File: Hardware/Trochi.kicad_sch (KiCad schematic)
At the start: 61 parts, among them IC1 ICM-42688-P, J1 JST-SH, J2 JST-SH, J3 JST PH, J4 JST-SH, J5 JST-SH, J6 JST_SH, Q1 AO3401A, Q2 AO3400A, Q3 AO3400A, Q4 AO3400A, Q5 AO3400A, Q6 AO3400A, SW1 SW_SPDT, U1 ME6211C33M5, U3 YX-SMD5020

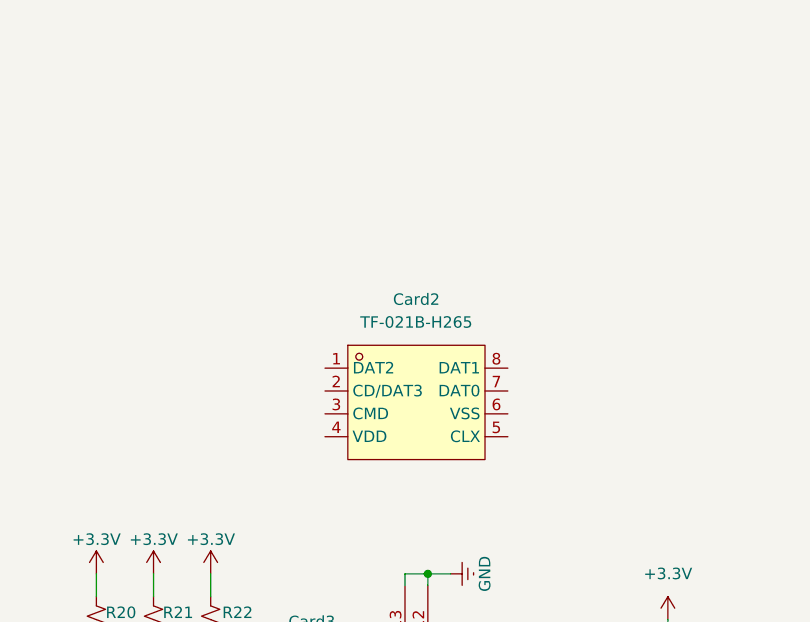
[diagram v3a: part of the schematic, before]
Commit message: feat: add updated TF-021B-H265 symbol to schematic
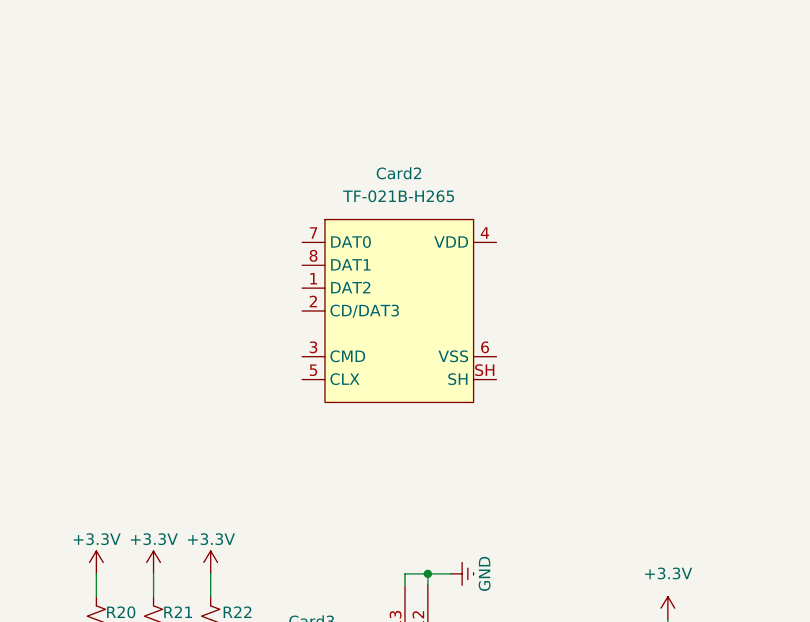
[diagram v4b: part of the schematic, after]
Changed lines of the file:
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@@
-	)
-	(symbol
-		(lib_id "trochi_sym:TF-021B-H265")
-		(at 106.68 255.27 0)
-		(unit 1)
-		(body_style 1)
-		(exclude_from_sim no)
-		(in_bom yes)
-		(on_board yes)
-		(in_pos_files yes)
-		(dnp no)
-		(fields_autoplaced yes)
-		(property "Reference" "Card2"
-			(at 102.87 243.84 0)
-			(show_name no)
-			(do_not_autoplace no)
-			(effects
-				(font
-					(size 1.27 1.27)
-				)
-			)
-		)
-		(property "Value" "TF-021B-H265"
-			(at 102.87 246.38 0)
-			(show_name no)
-			(do_not_autoplace no)
-			(effects
-				(font
-					(size 1.27 1.27)
-				)
-			)
-		)
-		(property "Footprint" "trochi_footprint:TF-SMD_TF-021B-H265"
-			(at 106.68 269.24 0)
-			(hide yes)
-			(show_name no)
-			(do_not_autoplace no)
-			(effects
-				(font
-					(size 1.27 1.27)
-				)
-			)
-		)
-		(property "Datasheet" "https://lcsc.com/product-detail/New-Arrivals_SOFNG-TF-021B-H265_C498185.html"
-			(at 106.68 271.78 0)
-			(hide yes)
-			(show_name no)
-			(do_not_autoplace no)
-			(effects
-				(font
-					(size 1.27 1.27)
-				)
-			)
-		)
-		(property "Description" ""
-			(at 106.68 255.27 0)
-			(hide yes)
-			(show_name no)
-			(do_not_autoplace no)
-			(effects
-				(font
-					(size 1.27 1.27)
-				)
-			)
-		)
-		(property "Manufacturer" "SOFNG(硕方)"
-			(at 106.68 274.32 0)
-			(hide yes)
-			(show_name no)
-			(do_not_autoplace no)
-			(effects
-				(font
-					(size 1.27 1.27)
-				)
-			)
-		)
-		(property "MPN" "TF-021B-H265"
-			(at 106.68 276.86 0)
-			(hide yes)
-			(show_name no)
-			(do_not_autoplace no)
-			(effects
-				(font
-					(size 1.27 1.27)
-				)
-			)
-		)
-		(property "LCSC Part" "C498185"
-			(at 106.68 279.4 0)
-			(hide yes)
-			(show_name no)
-			(do_not_autoplace no)
-			(effects
-				(font
-					(size 1.27 1.27)
-				)
-			)
-		)
-		(pin "1"
-		)
-		(pin "5"
-		)
-		(pin "7"
-		)
-		(pin "3"
-		)
-		(pin "4"
-		)
-		(pin "8"
-		)
-		(pin "6"
-		)
-		(pin "2"
-		)
-		(instances
-			(project "Trochi"
-				(path "/a5119cab-c33d-484e-b542-18705d0dc8d0"
-					(reference "Card2")
-					(unit 1)
-				)
-			)
-		)
 	)
 	(symbol
@@
 					(unit 1)
 				)
+			)
+		)
+	)
+	(symbol
+		(lib_id "trochi_sym:TF-021B-H265")
+		(at 104.14 243.84 0)
+		(unit 1)
+		(body_style 1)
+		(exclude_from_sim no)
+		(in_bom yes)
+		(on_board yes)
+		(in_pos_files yes)
+		(dnp no)
+		(fields_autoplaced yes)
+		(property "Reference" "Card2"
+			(at 100.965 229.87 0)
+			(show_name no)
+			(do_not_autoplace no)
+			(effects
+				(font
+					(size 1.27 1.27)
+				)
+			)
+		)
+		(property "Value" "TF-021B-H265"
+			(at 100.965 232.41 0)
+			(show_name no)
+			(do_not_autoplace no)
+			(effects
+				(font
+					(size 1.27 1.27)
+				)
+			)
+		)
+		(property "Footprint" "trochi_footprint:TF-SMD_TF-021B-H265"
+			(at 101.6 260.35 0)
+			(hide yes)
+			(show_name no)
+			(do_not_autoplace no)
+			(effects
+				(font
+					(size 1.27 1.27)
+				)
+			)
+		)
+		(property "Datasheet" "https://lcsc.com/product-detail/New-Arrivals_SOFNG-TF-021B-H265_C498185.html"
+			(at 101.6 262.89 0)
+			(hide yes)
+			(show_name no)
+			(do_not_autoplace no)
+			(effects
+				(font
+					(size 1.27 1.27)
+				)
+			)
+		)
+		(property "Description" ""
+			(at 104.14 243.84 0)
+			(hide yes)
+			(show_name no)
+			(do_not_autoplace no)
+			(effects
+				(font
+					(size 1.27 1.27)
+				)
+			)
+		)
+		(property "Manufacturer" "SOFNG(硕方)"
+			(at 101.6 265.43 0)
+			(hide yes)
+			(show_name no)
+			(do_not_autoplace no)
+			(effects
+				(font
+					(size 1.27 1.27)
+				)
+			)
+		)
+		(property "MPN" "TF-021B-H265"
+			(at 101.6 267.97 0)
+			(hide yes)
+			(show_name no)
+			(do_not_autoplace no)
+			(effects
+				(font
+					(size 1.27 1.27)
+				)
+			)
+		)
+		(property "LCSC Part" "C498185"
+			(at 101.6 270.51 0)
+			(hide yes)
+			(show_name no)
+			(do_not_autoplace no)
+			(effects
+				(font
+					(size 1.27 1.27)
+				)
+			)
+		)
+		(pin "2"
+		)
+		(pin "1"
+		)
+		(pin "3"
+		)
+		(pin "4"
+		)
+		(pin "5"
+		)
+		(pin "8"
+		)
+		(pin "6"
+		)
+		(pin "SH"
+		)
+		(pin "7"
+		)
+		(instances
+			(project "Trochi"
+				(path "/a5119cab-c33d-484e-b542-18705d0dc8d0"
+					(reference "Card2")
+					(unit 1)
+				)

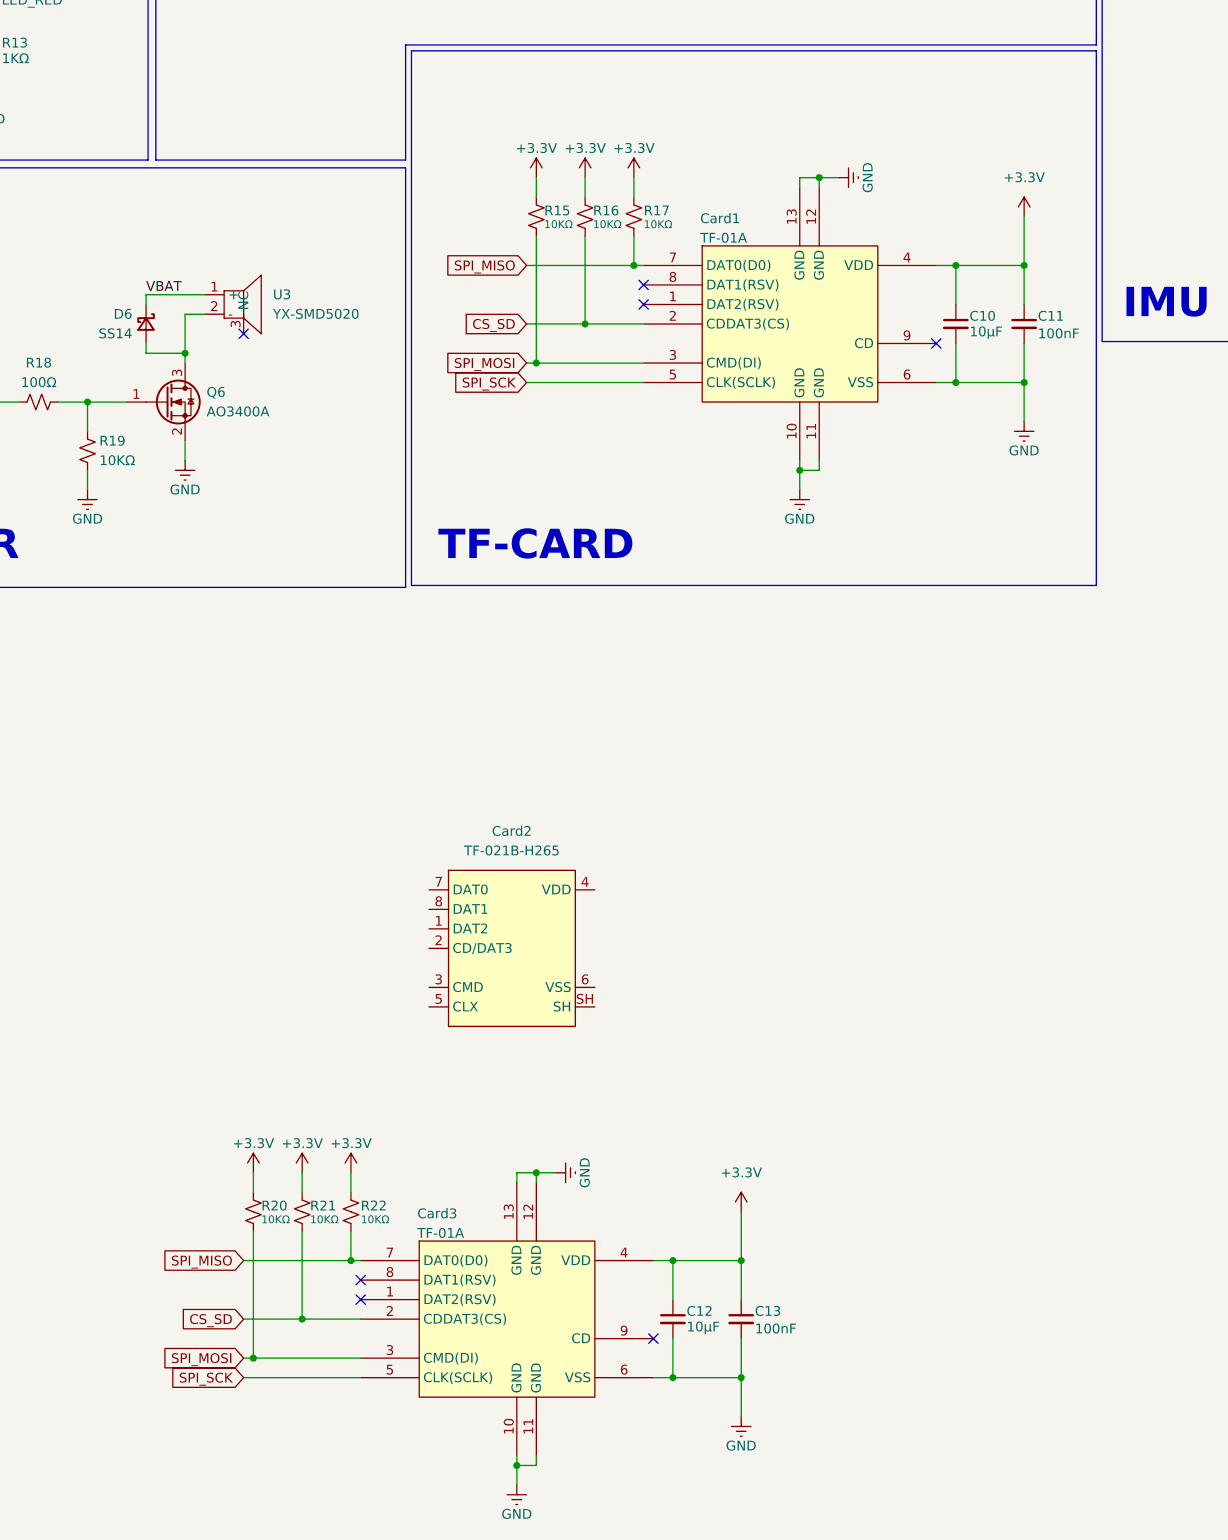
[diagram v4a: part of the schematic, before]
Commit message: feat: wire new SD card connections in schematic
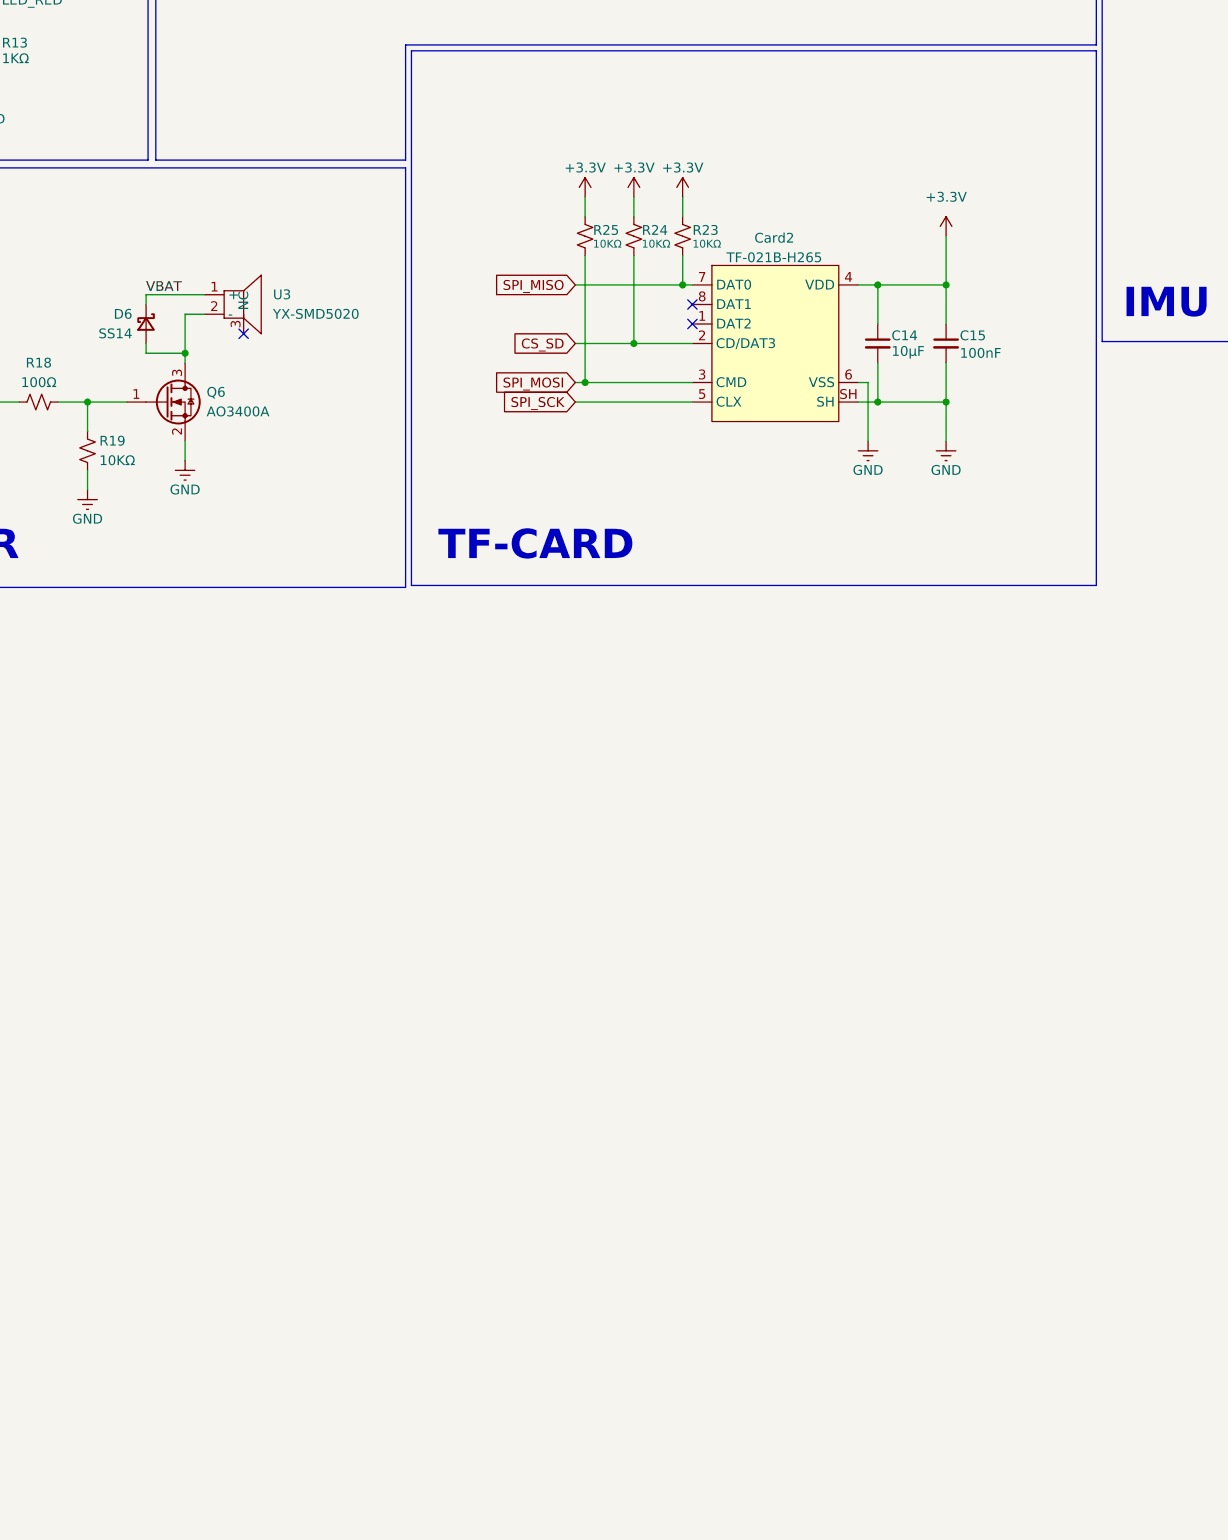
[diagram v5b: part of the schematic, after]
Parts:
- removed C10, C12: 10µF, Capacitor_SMD:C_0402_1005Metric, symbol Device:C_Small
- removed C11, C13: 100nF, Capacitor_SMD:C_0402_1005Metric, symbol Device:C_Small
- removed Card1, Card3: TF-01A, trochi_footprint:TF-SMD_TF-01A, symbol trochi_sym:TF-01A
- removed R15, R16, R17, R20, R21, R22: 10KΩ, Resistor_SMD:R_0402_1005Metric, symbol Device:R_Small_US
- added C14: 10µF, Capacitor_SMD:C_0402_1005Metric, symbol Device:C_Small
- added C15: 100nF, Capacitor_SMD:C_0402_1005Metric, symbol Device:C_Small
- added R23, R24, R25: 10KΩ, Resistor_SMD:R_0402_1005Metric, symbol Device:R_Small_US
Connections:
- net +3.3V: now also Card2.4 (VDD), C14.1, C15.1, R23.1, R24.1, R25.1
- net CS_SD: now also Card2.2 (CD/DAT3), R24.2
- net GND: now also Card2.6 (VSS), Card2.SH, C14.2, C15.2
- net SPI_MISO: now also Card2.7 (DAT0), R23.2
- net SPI_MOSI: now also Card2.3 (CMD), R25.2
- net SPI_SCK: now also Card2.5 (CLX)
- no-connect marks 10 -> 6
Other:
- moved on the sheet: Card2

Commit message: docs: add product details for TF-021B-H265 in schematic
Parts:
- Card2: LCSC (none) -> https://www.lcsc.com/product-detail/C498185.html?s_z=n_q_t_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; LCSC Part C498185 -> (none); Part Number (none) -> C498185
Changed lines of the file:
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@@
 			)
 		)
-		(property "LCSC Part" "C498185"
+		(property "Part Number" "C498185"
 			(at 135.89 191.77 0)
 			(hide yes)
 			(show_name no)
+			(do_not_autoplace no)
+			(effects
+				(font
+					(size 1.27 1.27)
+				)
+			)
+		)
+		(property "LCSC" "https://www.lcsc.com/product-detail/C498185.html?s_z=n_q_t_sd%2520card&spm=wm.fly.bg.22.xh___wm.ssy.tc.0.tz&lcsc_vid=RwJfAwcCQlFXAgdfFgNeAlIEFQVdBlQHFVEMUVIATwQxVlNeT1BcVVRQT1JWVjsOAxUeFF5JWBYZEEoKFBINSQcJGk4dAhYQHgILSBUTEhIaDgsI"
+			(at 138.43 165.1 0)
+			(hide yes)
+			(show_name no)

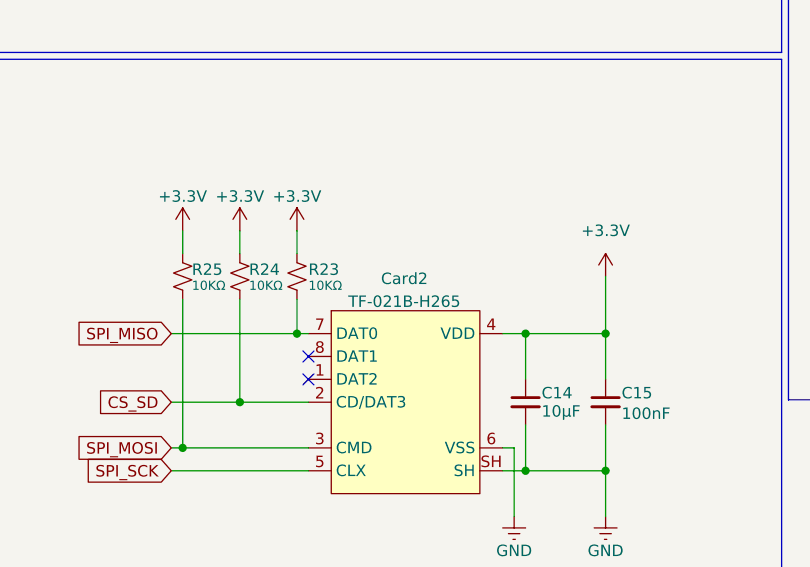
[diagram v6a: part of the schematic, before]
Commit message: fix: resolve ERC warnings by correcting pin electrical types
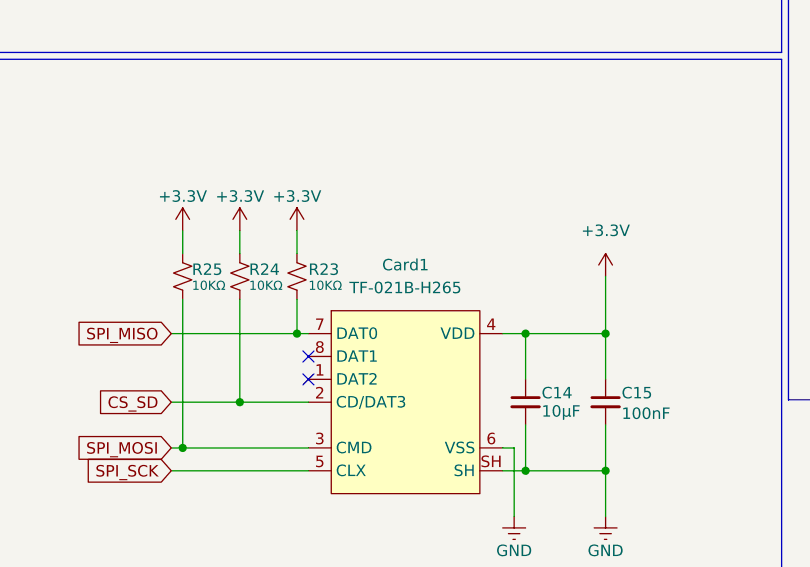
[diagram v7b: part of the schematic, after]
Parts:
- removed Card2: TF-021B-H265, trochi_footprint:TF-SMD_TF-021B-H265, symbol trochi_sym:TF-021B-H265
- added Card1: TF-021B-H265, trochi_footprint:TF-SMD_TF-021B-H265, symbol trochi_sym:TF-021B-H265
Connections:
- net +3.3V: now also Card1.4 (VDD)
- net CS_SD: now also Card1.2 (CD/DAT3)
- net GND: now also Card1.6 (VSS), Card1.SH
- net SPI_MISO: now also Card1.7 (DAT0)
- net SPI_MOSI: now also Card1.3 (CMD)
- net SPI_SCK: now also Card1.5 (CLX)
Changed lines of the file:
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@@
+	)
+	(symbol
+		(lib_id "trochi_sym:TF-021B-H265")
+		(at 138.43 165.1 0)
+		(unit 1)
+		(body_style 1)
+		(exclude_from_sim no)
+		(in_bom yes)
+		(on_board yes)
+		(in_pos_files yes)
+		(dnp no)
+		(fields_autoplaced yes)
+		(property "Reference" "Card1"
+			(at 135.255 151.13 0)
+			(show_name no)
+			(do_not_autoplace no)
+			(effects
+				(font
+					(size 1.27 1.27)
+				)
+			)
+		)
+		(property "Value" "TF-021B-H265"
+			(at 135.255 153.67 0)
+			(show_name no)
+			(do_not_autoplace no)
+			(effects
+				(font
+					(size 1.27 1.27)
+				)
+			)
+		)
+		(property "Footprint" "trochi_footprint:TF-SMD_TF-021B-H265"
+			(at 135.89 181.61 0)
+			(hide yes)
+			(show_name no)
+			(do_not_autoplace no)
+			(effects
+				(font
+					(size 1.27 1.27)
+				)
+			)
+		)
+		(property "Datasheet" "https://lcsc.com/product-detail/New-Arrivals_SOFNG-TF-021B-H265_C498185.html"
+			(at 135.89 184.15 0)
+			(hide yes)
+			(show_name no)
+			(do_not_autoplace no)
+			(effects
+				(font
+					(size 1.27 1.27)
+				)
+			)
+		)
+		(property "Description" ""
+			(at 138.43 165.1 0)
+			(hide yes)
+			(show_name no)
+			(do_not_autoplace no)
+			(effects
+				(font
+					(size 1.27 1.27)
+				)
+			)
+		)
+		(property "Manufacturer" "SOFNG(硕方)"
+			(at 135.89 186.69 0)
+			(hide yes)
+			(show_name no)
+			(do_not_autoplace no)
+			(effects
+				(font
+					(size 1.27 1.27)
+				)
+			)
+		)
+		(property "MPN" "TF-021B-H265"
+			(at 135.89 189.23 0)
+			(hide yes)
+			(show_name no)
+			(do_not_autoplace no)
+			(effects
+				(font
+					(size 1.27 1.27)
+				)
+			)
+		)
+		(property "LCSC Part" "C498185"
+			(at 135.89 191.77 0)
+			(hide yes)
+			(show_name no)
+			(do_not_autoplace no)
+			(effects
+				(font
+					(size 1.27 1.27)
+				)
+			)
+		)
+		(pin "SH"
+		)
+		(pin "3"
+		)
+		(pin "7"
+		)
+		(pin "5"
+		)
+		(pin "8"
+		)
+		(pin "6"
+		)
+		(pin "1"
+		)
+		(pin "2"
+		)
+		(pin "4"
+		)
+		(instances
+			(project "Trochi"
+				(path "/a5119cab-c33d-484e-b542-18705d0dc8d0"
+					(reference "Card1")
+					(unit 1)
+				)
+			)
+		)
 	)
 	(symbol
@@
 					(unit 1)
 				)
-			)
-		)
-	)
-	(symbol
-		(lib_id "trochi_sym:TF-021B-H265")
-		(at 138.43 165.1 0)
-		(unit 1)
-		(body_style 1)
-		(exclude_from_sim no)
-		(in_bom yes)
-		(on_board yes)
-		(in_pos_files yes)
-		(dnp no)
-		(property "Reference" "Card2"
-			(at 135.128 152.654 0)
-			(show_name no)
-			(do_not_autoplace no)
-			(effects
-				(font
-					(size 1.27 1.27)
-				)
-			)
-		)
-		(property "Value" "TF-021B-H265"
-			(at 135.128 155.194 0)
-			(show_name no)
-			(do_not_autoplace no)
-			(effects
-				(font
-					(size 1.27 1.27)
-				)
-			)
-		)
-		(property "Footprint" "trochi_footprint:TF-SMD_TF-021B-H265"
-			(at 135.89 181.61 0)
-			(hide yes)
-			(show_name no)
-			(do_not_autoplace no)
-			(effects
-				(font
-					(size 1.27 1.27)
-				)
-			)
-		)
-		(property "Datasheet" "https://lcsc.com/product-detail/New-Arrivals_SOFNG-TF-021B-H265_C498185.html"
-			(at 135.89 184.15 0)
-			(hide yes)
-			(show_name no)
-			(do_not_autoplace no)
-			(effects
-				(font
-					(size 1.27 1.27)
-				)
-			)
-		)
-		(property "Description" ""
-			(at 138.43 165.1 0)
-			(hide yes)
-			(show_name no)
-			(do_not_autoplace no)
-			(effects
-				(font
-					(size 1.27 1.27)
-				)
-			)
-		)
-		(property "Manufacturer" "SOFNG(硕方)"
-			(at 135.89 186.69 0)
-			(hide yes)
-			(show_name no)
-			(do_not_autoplace no)
-			(effects
-				(font
-					(size 1.27 1.27)
-				)
-			)
-		)
-		(property "MPN" "TF-021B-H265"
-			(at 135.89 189.23 0)
-			(hide yes)
-			(show_name no)
-			(do_not_autoplace no)
-			(effects
-				(font
-					(size 1.27 1.27)
-				)
-			)
-		)
-		(property "Part Number" "C498185"
-			(at 135.89 191.77 0)
-			(hide yes)
-			(show_name no)
-			(do_not_autoplace no)
-			(effects
-				(font
-					(size 1.27 1.27)
-				)
-			)
-		)
-		(property "LCSC" "https://www.lcsc.com/product-detail/C498185.html?s_z=n_q_t_sd%2520card&spm=wm.fly.bg.22.xh___wm.ssy.tc.0.tz&lcsc_vid=RwJfAwcCQlFXAgdfFgNeAlIEFQVdBlQHFVEMUVIATwQxVlNeT1BcVVRQT1JWVjsOAxUeFF5JWBYZEEoKFBINSQcJGk4dAhYQHgILSBUTEhIaDgsI"
-			(at 138.43 165.1 0)
-			(hide yes)
-			(show_name no)
-			(do_not_autoplace no)
-			(effects
-				(font
-					(size 1.27 1.27)
-				)
-			)
-		)
-		(pin "2"
-		)
-		(pin "1"
-		)
-		(pin "3"
-		)
-		(pin "4"
-		)
-		(pin "5"
-		)
-		(pin "8"
-		)
-		(pin "6"
-		)
-		(pin "SH"
-		)
-		(pin "7"
-		)
-		(instances
-			(project "Trochi"
-				(path "/a5119cab-c33d-484e-b542-18705d0dc8d0"
-					(reference "Card2")
-					(unit 1)
-				)
